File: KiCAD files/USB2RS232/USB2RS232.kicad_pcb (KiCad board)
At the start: 2 copper layers, 40 parts, among them J1 Reset jumper, J2 TTL port, J4 RS232, U5 MAX232

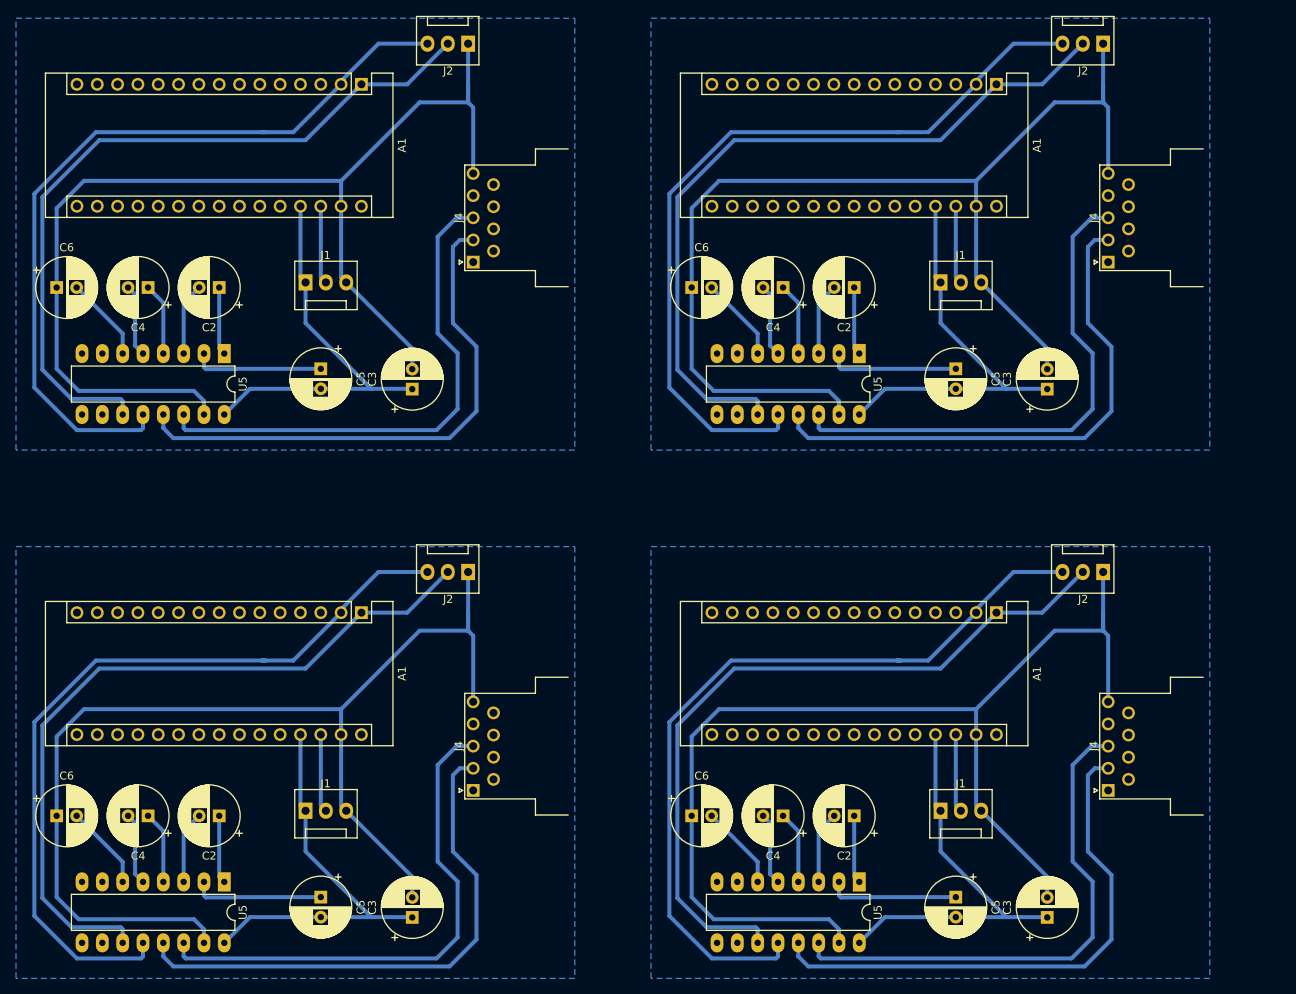
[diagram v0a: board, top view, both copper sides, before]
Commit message: Update USB2RS232.kicad_pcb
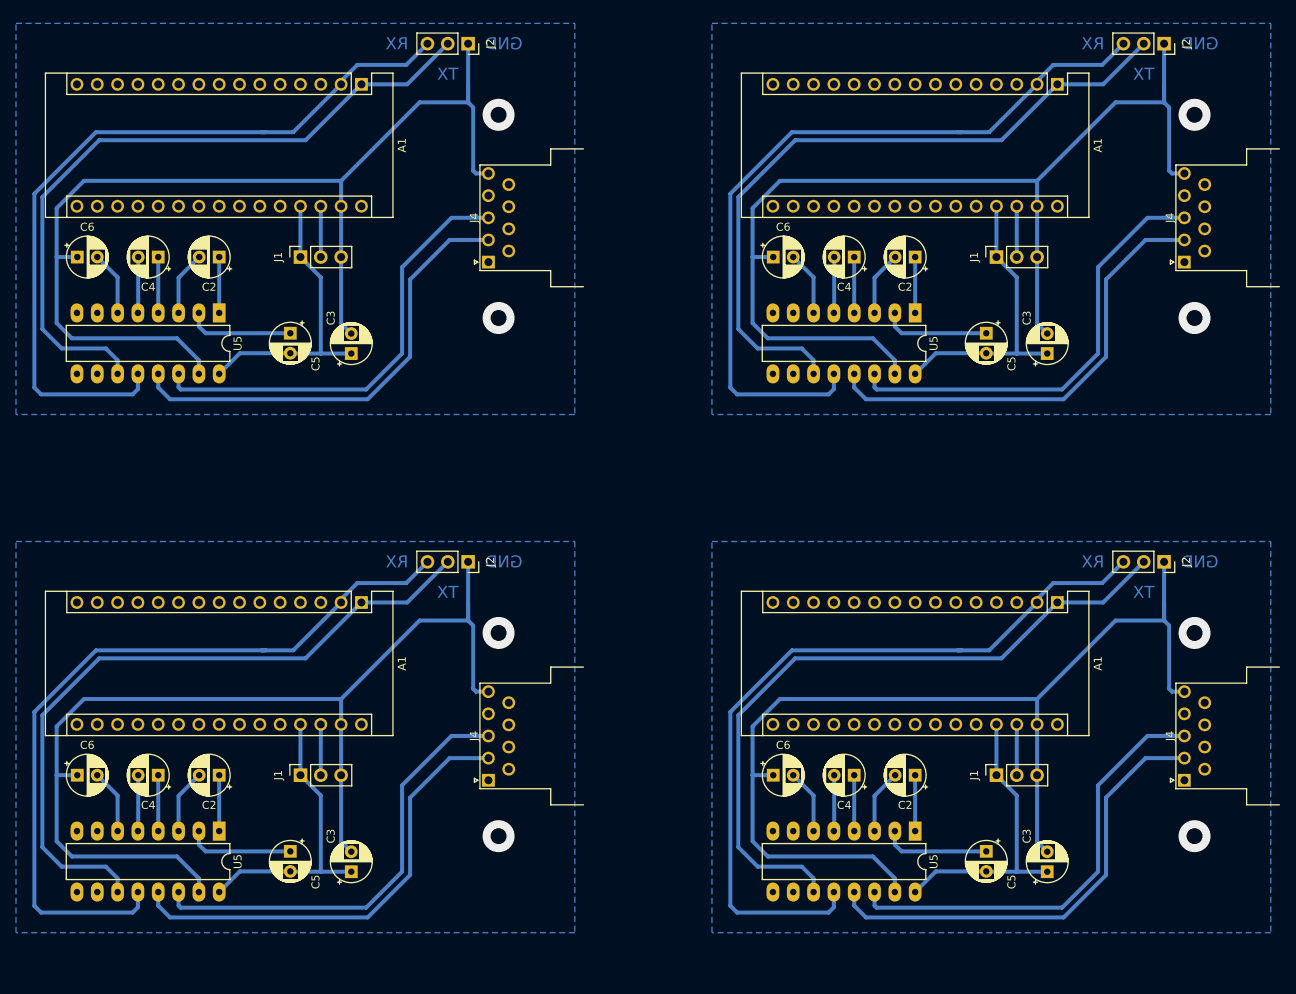
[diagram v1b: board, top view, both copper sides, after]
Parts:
- removed the A1 at (109.2, 106.0)
- removed the A1 at (188.6, 106.0)
- removed the A1 at (188.6, 40.0)
- removed the C2 at (91.4, 131.4)
- removed the C2 at (170.8, 131.4)
- removed the C2 at (91.4, 65.4)
- removed the C2 at (170.8, 65.4)
- removed the C3 at (194.9, 144.1)
- removed the C3 at (115.6, 144.1)
- removed the C3 at (115.6, 78.1)
- removed the C3 at (194.9, 78.1)
- removed the C4 at (161.9, 131.4)
- removed the C4 at (82.5, 131.4)
- removed the C4 at (82.5, 65.4)
- removed the C4 at (161.9, 65.4)
- removed the C5 at (183.5, 141.6)
- removed the C5 at (104.1, 141.6)
- removed the C5 at (104.1, 75.6)
- removed the C5 at (183.5, 75.6)
- removed the C6 at (71.1, 131.4)
- removed the C6 at (150.5, 131.4)
- removed the C6 at (71.1, 65.4)
- removed the C6 at (150.5, 65.4)
- removed the J1 at (102.2, 130.8)
- removed the J1 at (181.6, 130.8)
- removed the J1 at (102.2, 64.8)
- removed the J1 at (181.6, 64.8)
- removed the J2 at (122.6, 101.0)
- removed the J2 at (201.9, 101.0)
- removed the J2 at (122.6, 34.9)
- removed the J2 at (201.9, 34.9)
- removed the J4 at (123.2, 128.3)
- removed the J4 at (202.6, 128.3)
- removed the J4 at (202.6, 62.2)
- removed the U5 at (92.1, 139.7)
- removed the U5 at (171.4, 139.7)
- removed the U5 at (171.4, 73.7)
- added A1: Arduino_Nano_v3.x, Module:Arduino_Nano, F.Cu at (196.2, 104.8)
- added A1: Arduino_Nano_v3.x, Module:Arduino_Nano, F.Cu at (109.2, 104.8)
- added A1: Arduino_Nano_v3.x, Module:Arduino_Nano, F.Cu at (196.2, 40.0)
- added C2: 1uF, Capacitor_THT:CP_Radial_D5.0mm_P2.50mm, F.Cu at (178.4, 126.4)
- added C2: 1uF, Capacitor_THT:CP_Radial_D5.0mm_P2.50mm, F.Cu at (91.4, 126.4)
- added C2: 1uF, Capacitor_THT:CP_Radial_D5.0mm_P2.50mm, F.Cu at (178.4, 61.6)
- added C2: 1uF, Capacitor_THT:CP_Radial_D5.0mm_P2.50mm, F.Cu at (91.4, 61.6)
- added C3: 1uF, Capacitor_THT:CP_Radial_D5.0mm_P2.50mm, F.Cu at (194.9, 138.4)
- added C3: 1uF, Capacitor_THT:CP_Radial_D5.0mm_P2.50mm, F.Cu at (108.0, 138.4)
- added C3: 1uF, Capacitor_THT:CP_Radial_D5.0mm_P2.50mm, F.Cu at (194.9, 73.7)
- added C3: 1uF, Capacitor_THT:CP_Radial_D5.0mm_P2.50mm, F.Cu at (108.0, 73.7)
- added C4: 1uF, Capacitor_THT:CP_Radial_D5.0mm_P2.50mm, F.Cu at (170.8, 126.4)
- added C4: 1uF, Capacitor_THT:CP_Radial_D5.0mm_P2.50mm, F.Cu at (83.8, 126.4)
- added C4: 1uF, Capacitor_THT:CP_Radial_D5.0mm_P2.50mm, F.Cu at (170.8, 61.6)
- added C4: 1uF, Capacitor_THT:CP_Radial_D5.0mm_P2.50mm, F.Cu at (83.8, 61.6)
- added C5: 1uF, Capacitor_THT:CP_Radial_D5.0mm_P2.50mm, F.Cu at (187.3, 135.9)
- added C5: 1uF, Capacitor_THT:CP_Radial_D5.0mm_P2.50mm, F.Cu at (100.3, 135.9)
- added C5: 1uF, Capacitor_THT:CP_Radial_D5.0mm_P2.50mm, F.Cu at (187.3, 71.1)
- added C5: 1uF, Capacitor_THT:CP_Radial_D5.0mm_P2.50mm, F.Cu at (100.3, 71.1)
- added C6: 1uF, Capacitor_THT:CP_Radial_D5.0mm_P2.50mm, F.Cu at (160.7, 126.4)
- added C6: 1uF, Capacitor_THT:CP_Radial_D5.0mm_P2.50mm, F.Cu at (73.7, 126.4)
- added C6: 1uF, Capacitor_THT:CP_Radial_D5.0mm_P2.50mm, F.Cu at (160.7, 61.6)
- added C6: 1uF, Capacitor_THT:CP_Radial_D5.0mm_P2.50mm, F.Cu at (73.7, 61.6)
- added J1: Reset jumper, Connector_PinSocket_2.54mm:PinSocket_1x03_P2.54mm_Vertical, F.Cu at (188.6, 126.4)
- added J1: Reset jumper, Connector_PinSocket_2.54mm:PinSocket_1x03_P2.54mm_Vertical, F.Cu at (101.6, 126.4)
- added J1: Reset jumper, Connector_PinSocket_2.54mm:PinSocket_1x03_P2.54mm_Vertical, F.Cu at (188.6, 61.6)
- added J1: Reset jumper, Connector_PinSocket_2.54mm:PinSocket_1x03_P2.54mm_Vertical, F.Cu at (101.6, 61.6)
- added J2: TTL port, Connector_PinSocket_2.54mm:PinSocket_1x03_P2.54mm_Vertical, F.Cu at (209.6, 99.7)
- added J2: TTL port, Connector_PinSocket_2.54mm:PinSocket_1x03_P2.54mm_Vertical, F.Cu at (122.6, 99.7)
- added J2: TTL port, Connector_PinSocket_2.54mm:PinSocket_1x03_P2.54mm_Vertical, F.Cu at (209.6, 34.9)
- added J2: TTL port, Connector_PinSocket_2.54mm:PinSocket_1x03_P2.54mm_Vertical, F.Cu at (122.6, 34.9)
- added J4: RS232, Connector_Dsub:DSUB-9_Male_Horizontal_P2.77x2.54mm_EdgePinOffset9.40mm, F.Cu at (212.1, 127.0)
- added J4: RS232, Connector_Dsub:DSUB-9_Male_Horizontal_P2.77x2.54mm_EdgePinOffset9.40mm, F.Cu at (125.1, 127.0)
- added J4: RS232, Connector_Dsub:DSUB-9_Male_Horizontal_P2.77x2.54mm_EdgePinOffset9.40mm, F.Cu at (212.1, 62.2)
- added U5: MAX232, Package_DIP:DIP-16_W7.62mm_LongPads, F.Cu at (178.4, 133.3)
- added U5: MAX232, Package_DIP:DIP-16_W7.62mm_LongPads, F.Cu at (91.4, 133.3)
- added U5: MAX232, Package_DIP:DIP-16_W7.62mm_LongPads, F.Cu at (178.4, 68.6)
- moved U5 5.12 mm to (91.4, 68.6)
- moved J4 1.91 mm to (125.1, 62.2)
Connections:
- A1 pad 1: (no net) -> Net-(A1-Pad1)
- A1 pad 10: (no net) -> Net-(A1-Pad10)
- A1 pad 11: (no net) -> Net-(A1-Pad11)
- A1 pad 12: (no net) -> Net-(A1-Pad12)
- A1 pad 13: (no net) -> Net-(A1-Pad13)
- A1 pad 14: (no net) -> Net-(A1-Pad14)
- A1 pad 15: (no net) -> Net-(A1-Pad15)
- A1 pad 16: (no net) -> Net-(A1-Pad16)
- A1 pad 17: (no net) -> Net-(A1-Pad17)
- A1 pad 18: (no net) -> Net-(A1-Pad18)
- A1 pad 19: (no net) -> Net-(A1-Pad19)
- A1 pad 2: (no net) -> Net-(A1-Pad2)
- A1 pad 20: (no net) -> Net-(A1-Pad20)
- A1 pad 21: (no net) -> Net-(A1-Pad21)
- A1 pad 22: (no net) -> Net-(A1-Pad22)
- A1 pad 23: (no net) -> Net-(A1-Pad23)
- A1 pad 24: (no net) -> Net-(A1-Pad24)
- A1 pad 25: (no net) -> Net-(A1-Pad25)
- A1 pad 26: (no net) -> Net-(A1-Pad26)
- A1 pad 27: (no net) -> +5V
- A1 pad 28: (no net) -> Net-(A1-Pad28)
- A1 pad 29: (no net) -> GND
- A1 pad 3: (no net) -> Net-(A1-Pad3)
- A1 pad 30: (no net) -> Net-(A1-Pad30)
- A1 pad 4: (no net) -> Net-(A1-Pad4)
- A1 pad 5: (no net) -> Net-(A1-Pad5)
- A1 pad 6: (no net) -> Net-(A1-Pad6)
- A1 pad 7: (no net) -> Net-(A1-Pad7)
- A1 pad 8: (no net) -> Net-(A1-Pad8)
- A1 pad 9: (no net) -> Net-(A1-Pad9)
- J4 pad 1: (no net) -> Net-(J4-Pad1)
- J4 pad 2: (no net) -> Net-(J4-Pad2)
- J4 pad 3: (no net) -> Net-(J4-Pad3)
- J4 pad 4: (no net) -> Net-(J4-Pad4)
- J4 pad 5: (no net) -> GND
- J4 pad 6: (no net) -> Net-(J4-Pad6)
- J4 pad 7: (no net) -> Net-(J4-Pad7)
- J4 pad 8: (no net) -> Net-(J4-Pad8)
- J4 pad 9: (no net) -> Net-(J4-Pad9)
- U5 pad 1: (no net) -> Net-(C2-Pad1)
- U5 pad 10: (no net) -> Net-(U5-Pad10)
- U5 pad 11: (no net) -> Net-(A1-Pad1)
- U5 pad 12: (no net) -> Net-(A1-Pad2)
- U5 pad 13: (no net) -> Net-(J4-Pad2)
- U5 pad 14: (no net) -> Net-(J4-Pad3)
- U5 pad 15: (no net) -> GND
- U5 pad 16: (no net) -> +5V
- U5 pad 2: (no net) -> Net-(C5-Pad1)
- U5 pad 3: (no net) -> Net-(C2-Pad2)
- U5 pad 4: (no net) -> Net-(C4-Pad1)
- U5 pad 5: (no net) -> Net-(C4-Pad2)
- U5 pad 6: (no net) -> Net-(C6-Pad2)
- U5 pad 7: (no net) -> Net-(U5-Pad7)
- U5 pad 8: (no net) -> Net-(U5-Pad8)
- U5 pad 9: (no net) -> Net-(U5-Pad9)
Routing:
- net (no net): track 1784.4 -> 1583.1 mm, vias 0 -> 8
- net +5V: track 51.3 -> 37.1 mm
- net Net-(J4-Pad2): track 67.4 -> 57.5 mm
- net GND: track 144.7 -> 135.3 mm
- net Net-(J4-Pad3): track 65.1 -> 55.8 mm
- net Net-(A1-Pad1): track 93.6 -> 87.8 mm
- net Net-(A1-Pad28): track 10.5 -> 6.35 mm
- net Net-(C5-Pad1): track 16.4 -> 13.5 mm
- net Net-(C6-Pad2): track 10.6 -> 8.04 mm
- net Net-(A1-Pad2): track 99.4 -> 97.3 mm
- net Net-(C4-Pad1): track 9.04 -> 6.98 mm
- net Net-(C4-Pad2): track 9.03 -> 7.00 mm
- net Net-(C2-Pad1): track 8.52 -> 6.98 mm
- net Net-(C2-Pad2): track 9.06 -> 8.05 mm
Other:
- board text added: "GND"
- board text added: "RX"
- board text added: "TX"
